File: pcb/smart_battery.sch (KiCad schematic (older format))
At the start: 37 parts, among them J11 Conn_01x05_RTC, J12 Conn_HtrTh, J13 Conn_BattTh, Q1 MMBT5551L, Q2 MMBT5551L, U1 SPX3819M5-L-3-3, U10 FEATHER_M0_ADALOGGER, U11 FEATHERWING_HEATER_RELAY, U12 FEATHERWING_ETHERNET, U13 FEATHERWING_MINI_RELAY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

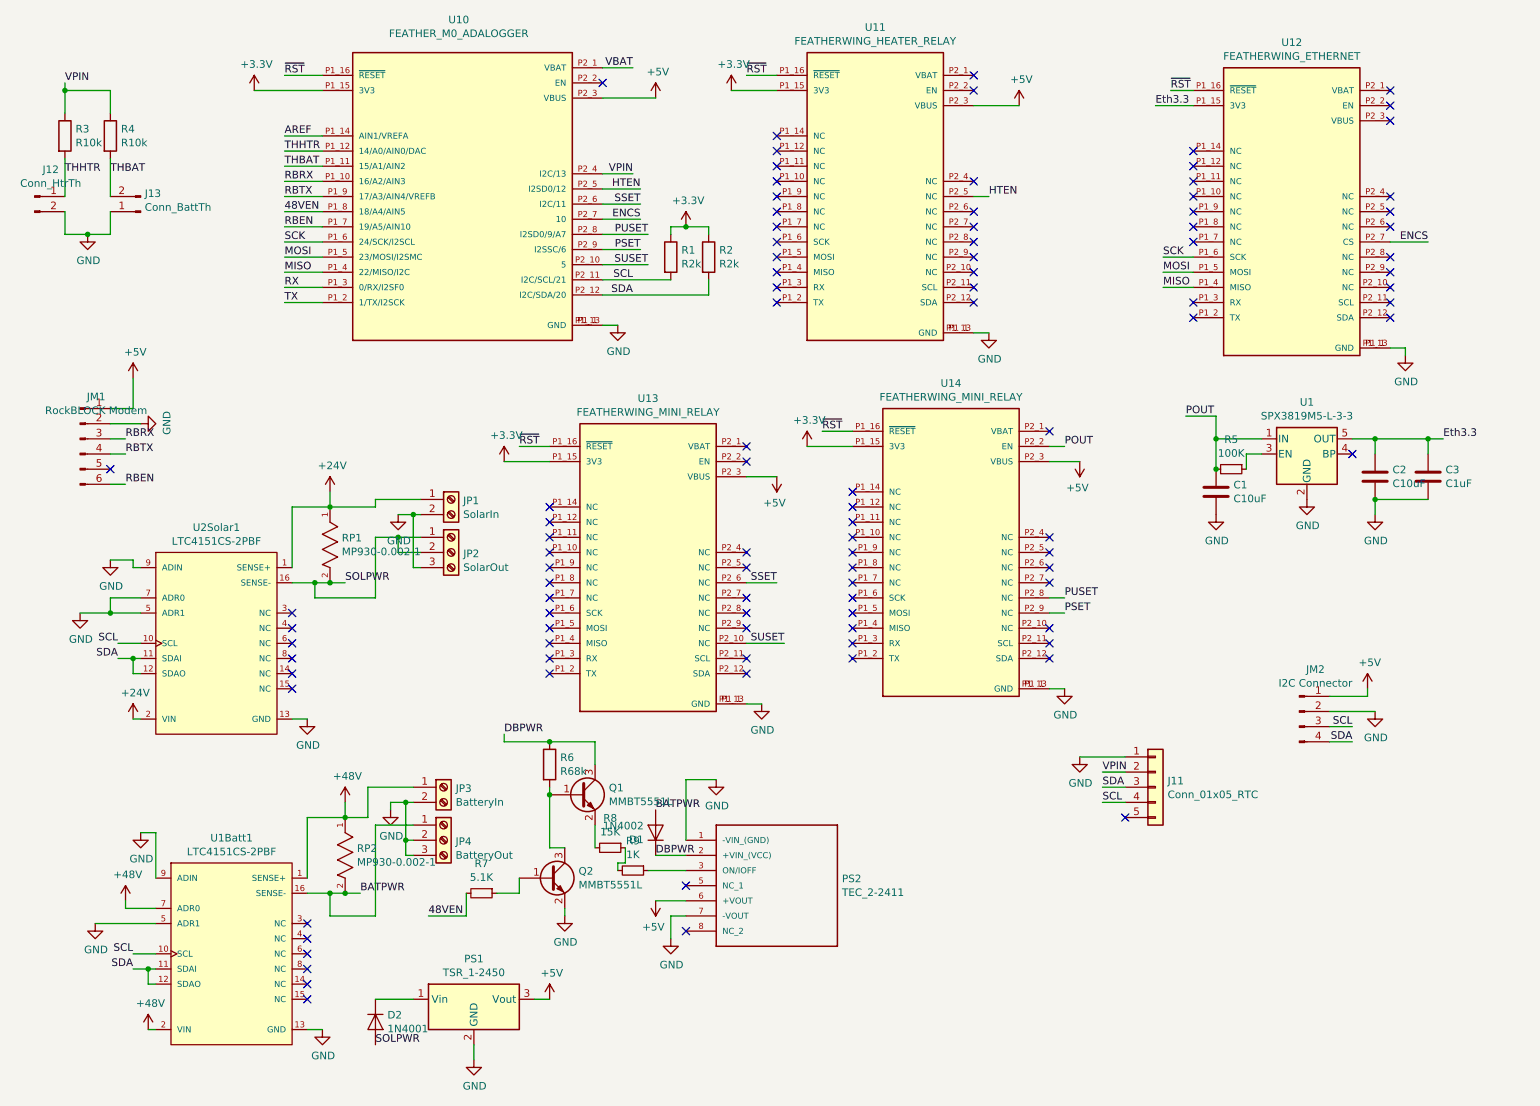
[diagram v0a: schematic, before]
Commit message: Fixed Sean comments, still need to redo the PCB
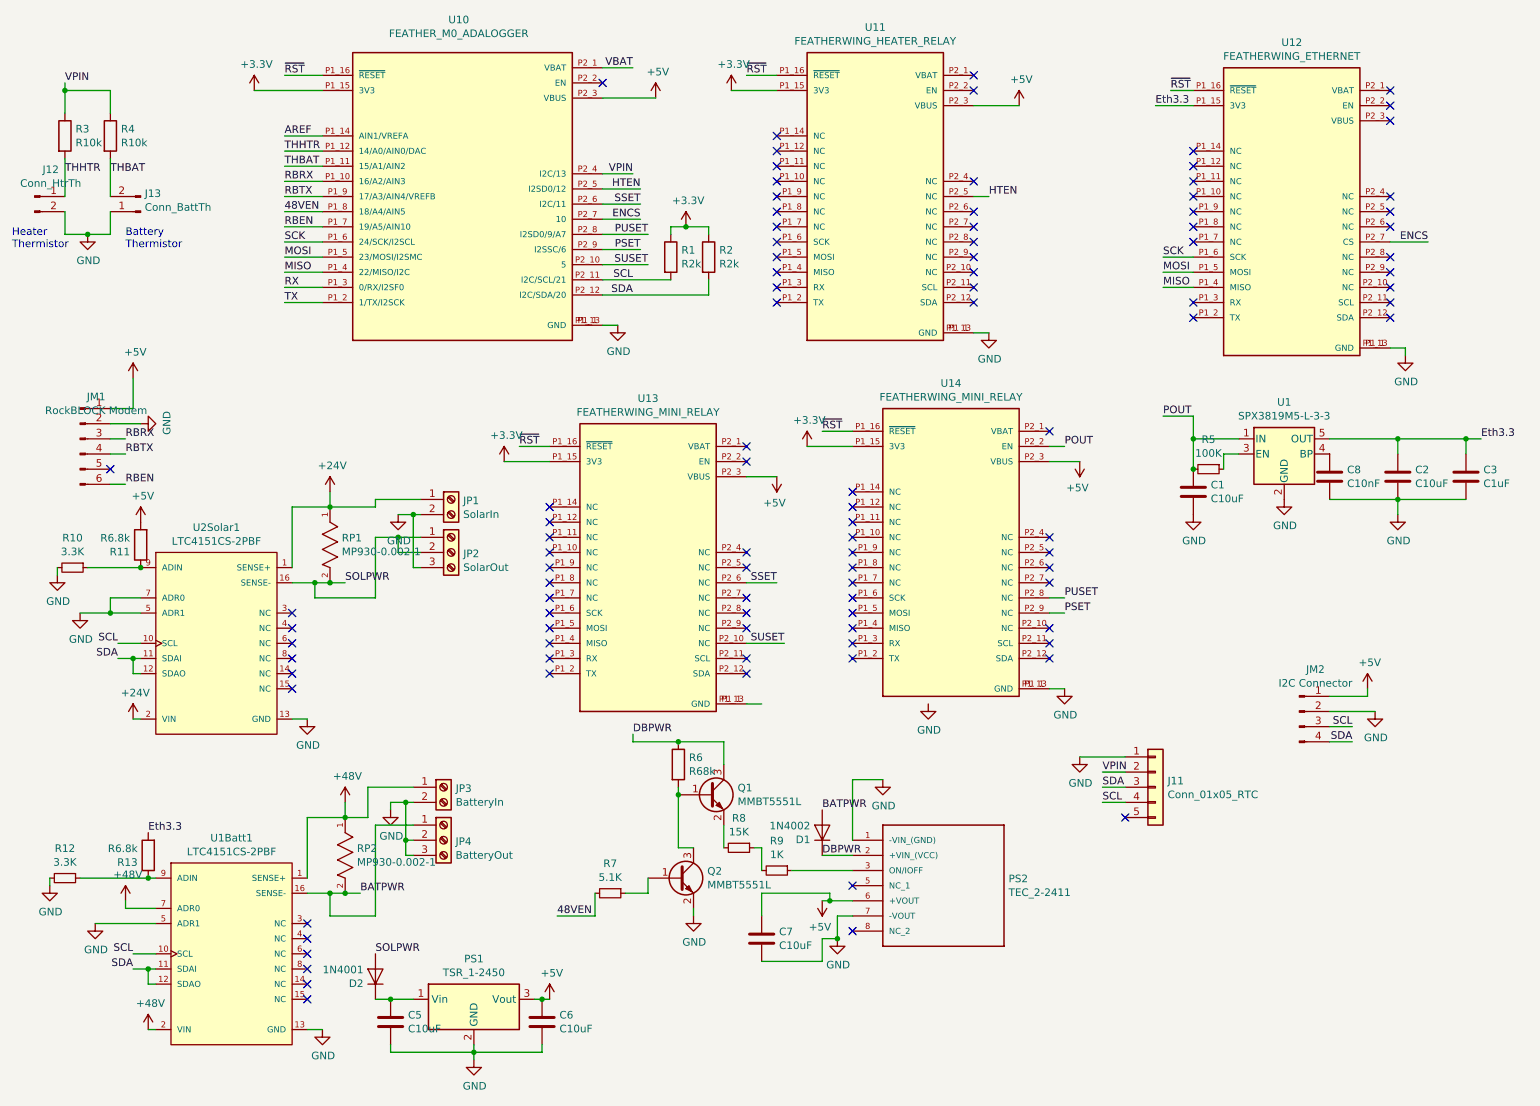
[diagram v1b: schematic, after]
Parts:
- added C5, C6, C7: C10uF, Capacitor_SMD:C_0805_2012Metric, symbol Device:C
- added C8: C10nF, Capacitor_SMD:C_0805_2012Metric, symbol Device:C
- added R10, R12: 3.3K, Resistor_SMD:R_0805_2012Metric, symbol Device:R_Small
- added R11, R13: R6.8k, Resistor_SMD:R_0805_2012Metric, symbol Device:R
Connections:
- net +5V: now also C6.1, C7.1, R11.2
- net Eth3.3: now also R13.2
- net GND: now also C5.2, C6.2, C7.2, C8.2, R10.2, R12.2; no longer U13.P1_1 (GND), U13.P1_13 (GND), U1Batt1.9 (ADIN), U2Solar1.9 (ADIN)
- net at U1.4 (BP): now also C8.1
- net at D2.1 (K), PS1.1 (Vin): now also C5.1
- new net: R12.1, R13.1, U1Batt1.9 (ADIN)
- new net: R10.1, R11.1, U2Solar1.9 (ADIN)
- new net: U13.P1_1 (GND), U13.P1_13 (GND)
- no-connect marks 101 -> 100
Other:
- note added: "Battery\nThermistor\n"
- note added: "Heater\nThermistor\n"
- moved on the sheet: C1, C2, C3, D1, D2, PS2, Q1, Q2, R5, R6, R7, R8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

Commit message: Added power symbols instead of labels for power buses
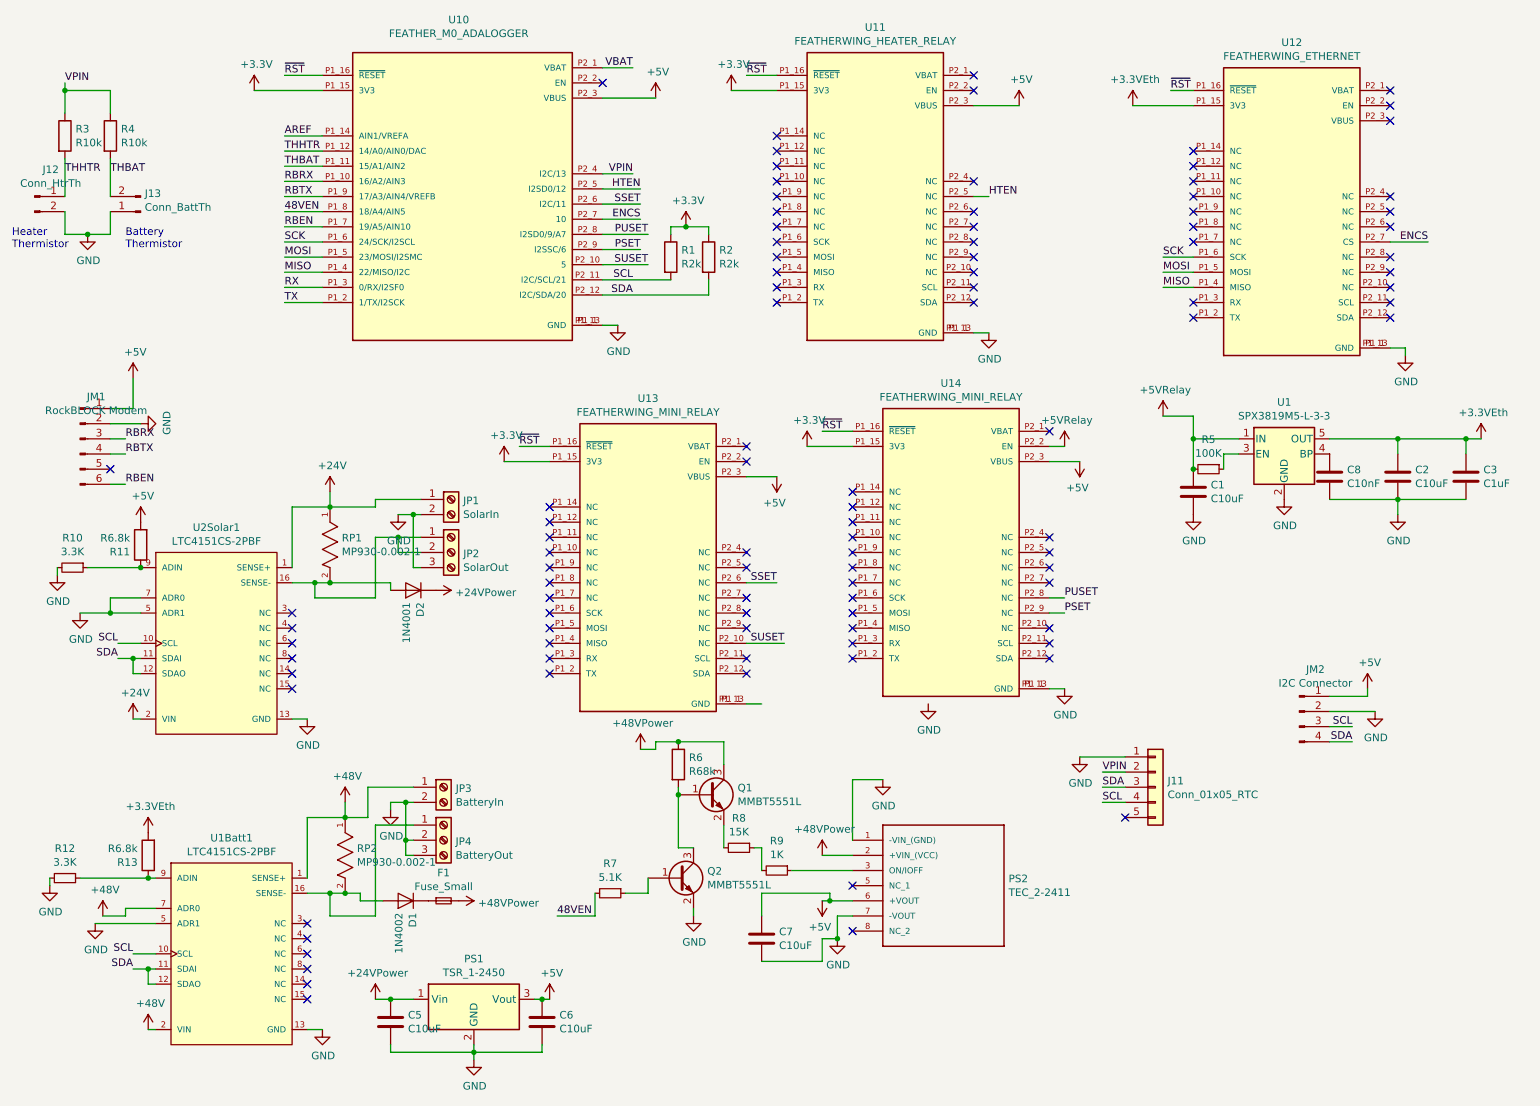
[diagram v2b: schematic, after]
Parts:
- added F1: Fuse_Small, symbol Device:Fuse_Small
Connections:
- net Eth3.3 is gone; now on net +48V: C2.1, C3.1, R13.2, U1.5 (OUT), U12.P1_15 (3V3)
- net POUT is gone; now on net +48V: C1.1, R5.2, U1.1 (IN), U14.P2_2 (EN)
- net +48V: now also C5.1, D2.1 (K), PS1.1 (Vin), PS2.2 (+VIN_(VCC)), Q1.3 (C), R6.1, F1.2
- net BATPWR: no longer names the net of D1.2 (A), JP4.1 (Pin_1), RP2.2, U1Batt1.16 (SENSE-)
- removed net DBPWR: D1.1 (K), PS2.2 (+VIN_(VCC)), Q1.3 (C), R6.1
- net SOLPWR: no longer names the net of D2.2 (A), JP2.1 (Pin_1), JP2.2 (Pin_2), RP1.2, U2Solar1.16 (SENSE-)
- new net: D1.1 (K), F1.1
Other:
- moved on the sheet: D1, D2
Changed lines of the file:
@@
 L power:+48V #PWR05
 U 1 1 6010A445
-P 1300 6400
-F 0 "#PWR05" H 1300 6250 50  0001 C CNN
-F 1 "+48V" H 1315 6573 50  0000 C CNN
-F 2 "" H 1300 6400 50  0001 C CNN
-F 3 "" H 1300 6400 50  0001 C CNN
-	1    1300 6400
-	1    0    0    -1
-$EndComp
-Wire Wire Line
-	1300 6400 1300 6450
+P 1150 6500
+F 0 "#PWR05" H 1150 6350 50  0001 C CNN
+F 1 "+48V" H 1165 6673 50  0000 C CNN
+F 2 "" H 1150 6500 50  0001 C CNN
+F 3 "" H 1150 6500 50  0001 C CNN
+	1    1150 6500
+	1    0    0    -1
+$EndComp
 Wire Wire Line
 	1300 6450 1500 6450
@@
 	-1   0    0    1
 $EndComp
-Text Label 7500 3400 0    50   ~ 0
-POUT
 $Comp
 L Connector_Generic:Conn_01x05 J11
@@
 Wire Wire Line
 	10250 3350 10150 3350
-Text Label 8100 1150 0    50   ~ 0
-Eth3.3
 $Comp
 L Device:R_Small R5
@@
 	1    0    0    -1
 $EndComp
-Text Label 8150 3200 0    50   ~ 0
-POUT
 Wire Wire Line
 	8150 3200 8350 3200
@@
 	2850 6350 2750 6350
 Connection ~ 2750 6350
-Text Label 5900 5800 0    50   ~ 0
-BATPWR
-Text Label 2850 6350 0    50   ~ 0
-BATPWR
-Text Label 2750 4300 0    50   ~ 0
-SOLPWR
-Wire Wire Line
-	2750 4300 2650 4300
 Connection ~ 2650 4300
-Text Label 2950 6750 0    50   ~ 0
-SOLPWR
 Wire Wire Line
 	2950 7050 3050 7050
@@
 	1    0    0    -1
 $EndComp
-Wire Wire Line
-	4650 5300 4650 5350
-Wire Wire Line
-	4650 5350 4950 5350
 $Comp
 L Device:R R6
@@
 Wire Wire Line
 	5250 5350 5250 5500
-Connection ~ 4950 5350
 $Comp
 L power:+5V #PWR0104
@@
 Wire Wire Line
 	8350 1050 8200 1050
-Wire Wire Line
-	8350 1150 8100 1150
 NoConn ~ 6900 950
 NoConn ~ 9650 1050
@@
 L Diode:1N4001 D2
 U 1 1 60267D7A
-P 2950 6900
-F 0 "D2" V 2904 6979 50  0000 L CNN
-F 1 "1N4001" V 2995 6979 50  0000 L CNN
-F 2 "Diode_THT:D_DO-41_SOD81_P10.16mm_Horizontal" H 2950 6725 50  0001 C CNN
-F 3 "http://www.vishay.com/docs/88503/1n4001.pdf" H 2950 6900 50  0001 C CNN
-	1    2950 6900
-	0    -1   -1   0
+P 3200 4350
+F 0 "D2" V 3154 4429 50  0000 L CNN
+F 1 "1N4001" V 3245 4429 50  0000 L CNN
+F 2 "Diode_THT:D_DO-41_SOD81_P10.16mm_Horizontal" H 3200 4175 50  0001 C CNN
+F 3 "http://www.vishay.com/docs/88503/1n4001.pdf" H 3200 4350 50  0001 C CNN
+	1    3200 4350
+	-1   0    0    1
 $EndComp
 $Comp
 L Diode:1N4002 D1
 U 1 1 602681D6
-P 5900 5950
-F 0 "D1" V 5854 6029 50  0000 L CNN
-F 1 "1N4002" V 5945 6029 50  0000 L CNN
-F 2 "Diode_THT:D_DO-41_SOD81_P10.16mm_Horizontal" H 5900 5775 50  0001 C CNN
-F 3 "http://www.vishay.com/docs/88503/1n4001.pdf" H 5900 5950 50  0001 C CNN
-	1    5900 5950
-	0    -1   -1   0
-$EndComp
-Text Label 4650 5300 0    50   ~ 0
-DBPWR
-Text Label 5900 6100 0    50   ~ 0
-DBPWR
+P 3150 6400
+F 0 "D1" V 3104 6479 50  0000 L CNN
+F 1 "1N4002" V 3195 6479 50  0000 L CNN
+F 2 "Diode_THT:D_DO-41_SOD81_P10.16mm_Horizontal" H 3150 6225 50  0001 C CNN
+F 3 "http://www.vishay.com/docs/88503/1n4001.pdf" H 3150 6400 50  0001 C CNN
+	1    3150 6400
+	-1   0    0    1
+$EndComp
 Wire Wire Line
 	4950 5700 4950 6050
@@
 	1450 6250 1500 6250
 Connection ~ 1450 6250
-Text Label 10250 3350 0    50   ~ 0
-Eth3.3
-Text Label 1450 5950 0    50   ~ 0
-Eth3.3
+Wire Wire Line
+	2850 6350 2850 6400
+$Comp
+L eec:+48VPower #PWR?
+U 1 1 603099AD
+P 5900 6100
+F 0 "#PWR?" H 5900 5950 50  0001 C CNN
+F 1 "+48VPower" H 5915 6273 50  0000 C CNN
+F 2 "" H 5900 6100 50  0001 C CNN
+F 3 "" H 5900 6100 50  0001 C CNN
+	1    5900 6100
+	1    0    0    -1
+$EndComp
+Wire Wire Line
+	2850 6400 3000 6400
+$Comp
+L Device:Fuse_Small F1
+U 1 1 60316340
+P 3400 6400
+F 0 "F1" H 3400 6585 50  0000 C CNN
+F 1 "Fuse_Small" H 3400 6494 50  0000 C CNN
+F 2 "" H 3400 6400 50  0001 C CNN
+F 3 "~" H 3400 6400 50  0001 C CNN
+	1    3400 6400
+	1    0    0    -1
+$EndComp
+$Comp
+L eec:+48VPower #PWR?
+U 1 1 60316928
+P 3500 6400
+F 0 "#PWR?" H 3500 6250 50  0001 C CNN
+F 1 "+48VPower" V 3515 6528 50  0000 L CNN
+F 2 "" H 3500 6400 50  0001 C CNN
+F 3 "" H 3500 6400 50  0001 C CNN
+	1    3500 6400
+	0    1    1    0
+$EndComp
+$Comp
+L eec:+48VPower #PWR?
+U 1 1 60316F04
+P 4700 5400
+F 0 "#PWR?" H 4700 5250 50  0001 C CNN
+F 1 "+48VPower" H 4715 5573 50  0000 C CNN
+F 2 "" H 4700 5400 50  0001 C CNN
+F 3 "" H 4700 5400 50  0001 C CNN
+	1    4700 5400
+	1    0    0    -1
+$EndComp
+Wire Wire Line
+	4700 5400 4800 5400
+Wire Wire Line
+	4800 5400 4800 5350
+Wire Wire Line
+	4800 5350 4950 5350
+Connection ~ 4950 5350
+Wire Wire Line
+	3050 4300 3050 4350
+Wire Wire Line
+	2650 4300 3050 4300
+$Comp
+L eec:+24VPower #PWR?
+U 1 1 6033DA59
+P 3350 4350
+F 0 "#PWR?" H 3350 4200 50  0001 C CNN
+F 1 "+24VPower" V 3365 4478 50  0000 L CNN
+F 2 "" H 3350 4350 50  0001 C CNN
+F 3 "" H 3350 4350 50  0001 C CNN
+	1    3350 4350
+	0    1    1    0
+$EndComp
+$Comp
+L eec:+24VPower #PWR?
+U 1 1 6033E548
+P 2950 7050
+F 0 "#PWR?" H 2950 6900 50  0001 C CNN
+F 1 "+24VPower" H 2965 7223 50  0000 C CNN
+F 2 "" H 2950 7050 50  0001 C CNN
+F 3 "" H 2950 7050 50  0001 C CNN
+	1    2950 7050
+	1    0    0    -1
+$EndComp
+Wire Wire Line
+	1300 6450 1300 6500
+Wire Wire Line
+	1300 6500 1150 6500
+$Comp
+L eec:+5VRelay #PWR?
+U 1 1 6038C736
+P 7500 3400
+F 0 "#PWR?" H 7500 3250 50  0001 C CNN
+F 1 "+5VRelay" H 7515 3573 50  0000 C CNN
+F 2 "" H 7500 3400 50  0001 C CNN
+F 3 "" H 7500 3400 50  0001 C CNN
+	1    7500 3400
+	1    0    0    -1
+$EndComp
+$Comp
+L eec:+5VRelay #PWR?
+U 1 1 6038C83C
+P 8150 3200
+F 0 "#PWR?" H 8150 3050 50  0001 C CNN
+F 1 "+5VRelay" H 8165 3373 50  0000 C CNN
+F 2 "" H 8150 3200 50  0001 C CNN
+F 3 "" H 8150 3200 50  0001 C CNN
+	1    8150 3200
+	1    0    0    -1
+$EndComp
+$Comp
+L eec:+3.3VEth #PWR?
+U 1 1 6039A381
+P 10250 3350
+F 0 "#PWR?" H 10250 3200 50  0001 C CNN
+F 1 "+3.3VEth" H 10265 3523 50  0000 C CNN
+F 2 "" H 10250 3350 50  0001 C CNN
+F 3 "" H 10250 3350 50  0001 C CNN
+	1    10250 3350
+	1    0    0    -1
+$EndComp
+$Comp
+L eec:+3.3VEth #PWR?
+U 1 1 6039A683
+P 1450 5950
+F 0 "#PWR?" H 1450 5800 50  0001 C CNN
+F 1 "+3.3VEth" H 1465 6123 50  0000 C CNN
+F 2 "" H 1450 5950 50  0001 C CNN
+F 3 "" H 1450 5950 50  0001 C CNN
+	1    1450 5950
+	1    0    0    -1
+$EndComp
+$Comp
+L eec:+3.3VEth #PWR?
+U 1 1 6039AA3D
+P 7950 1150
+F 0 "#PWR?" H 7950 1000 50  0001 C CNN
+F 1 "+3.3VEth" H 7965 1323 50  0000 C CNN
+F 2 "" H 7950 1150 50  0001 C CNN
+F 3 "" H 7950 1150 50  0001 C CNN
+	1    7950 1150
+	1    0    0    -1
+$EndComp
+Wire Wire Line
+	7950 1150 8350 1150
 $EndSCHEMATC

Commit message: Routed the new layout just need ground plane
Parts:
- added F2: Fuse_Small, Fuse:Fuseholder_Cylinder-5x20mm_Schurter_0031_8201_Horizontal_Open, symbol Device:Fuse_Small
- F1: footprint (none) -> Fuse:Fuseholder_Cylinder-5x20mm_Schurter_0031_8201_Horizontal_Open
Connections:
- net +48V: now also F2.1; no longer D2.1 (K)
- new net: D2.1 (K), F2.2
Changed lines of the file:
@@
 $EndComp
 $Comp
-L power:GND #PWR?
+L power:GND #PWR0117
 U 1 1 60405690
 P 800 6300
-F 0 "#PWR?" H 800 6050 50  0001 C CNN
+F 0 "#PWR0117" H 800 6050 50  0001 C CNN
 F 1 "GND" H 805 6127 50  0000 C CNN
 F 2 "" H 800 6300 50  0001 C CNN
@@
 	2850 6350 2850 6400
 $Comp
-L eec:+48VPower #PWR?
+L eec:+48VPower #PWR0118
 U 1 1 603099AD
 P 5900 6100
-F 0 "#PWR?" H 5900 5950 50  0001 C CNN
+F 0 "#PWR0118" H 5900 5950 50  0001 C CNN
 F 1 "+48VPower" H 5915 6273 50  0000 C CNN
 F 2 "" H 5900 6100 50  0001 C CNN
@@
 F 0 "F1" H 3400 6585 50  0000 C CNN
 F 1 "Fuse_Small" H 3400 6494 50  0000 C CNN
-F 2 "" H 3400 6400 50  0001 C CNN
+F 2 "Fuse:Fuseholder_Cylinder-5x20mm_Schurter_0031_8201_Horizontal_Open" H 3400 6400 50  0001 C CNN
 F 3 "~" H 3400 6400 50  0001 C CNN
 	1    3400 6400
@@
 $EndComp
 $Comp
-L eec:+48VPower #PWR?
+L eec:+48VPower #PWR0119
 U 1 1 60316928
 P 3500 6400
-F 0 "#PWR?" H 3500 6250 50  0001 C CNN
+F 0 "#PWR0119" H 3500 6250 50  0001 C CNN
 F 1 "+48VPower" V 3515 6528 50  0000 L CNN
 F 2 "" H 3500 6400 50  0001 C CNN
@@
 $EndComp
 $Comp
-L eec:+48VPower #PWR?
+L eec:+48VPower #PWR0120
 U 1 1 60316F04
 P 4700 5400
-F 0 "#PWR?" H 4700 5250 50  0001 C CNN
+F 0 "#PWR0120" H 4700 5250 50  0001 C CNN
 F 1 "+48VPower" H 4715 5573 50  0000 C CNN
 F 2 "" H 4700 5400 50  0001 C CNN
@@
 	2650 4300 3050 4300
 $Comp
-L eec:+24VPower #PWR?
+L eec:+24VPower #PWR0121
 U 1 1 6033DA59
-P 3350 4350
-F 0 "#PWR?" H 3350 4200 50  0001 C CNN
-F 1 "+24VPower" V 3365 4478 50  0000 L CNN
-F 2 "" H 3350 4350 50  0001 C CNN
-F 3 "" H 3350 4350 50  0001 C CNN
-	1    3350 4350
+P 3400 4750
+F 0 "#PWR0121" H 3400 4600 50  0001 C CNN
+F 1 "+24VPower" V 3415 4878 50  0000 L CNN
+F 2 "" H 3400 4750 50  0001 C CNN
+F 3 "" H 3400 4750 50  0001 C CNN
+	1    3400 4750
 	0    1    1    0
 $EndComp
 $Comp
-L eec:+24VPower #PWR?
+L eec:+24VPower #PWR0122
 U 1 1 6033E548
 P 2950 7050
-F 0 "#PWR?" H 2950 6900 50  0001 C CNN
+F 0 "#PWR0122" H 2950 6900 50  0001 C CNN
 F 1 "+24VPower" H 2965 7223 50  0000 C CNN
 F 2 "" H 2950 7050 50  0001 C CNN
@@
 	1300 6500 1150 6500
 $Comp
-L eec:+5VRelay #PWR?
+L eec:+5VRelay #PWR0123
 U 1 1 6038C736
 P 7500 3400
-F 0 "#PWR?" H 7500 3250 50  0001 C CNN
+F 0 "#PWR0123" H 7500 3250 50  0001 C CNN
 F 1 "+5VRelay" H 7515 3573 50  0000 C CNN
 F 2 "" H 7500 3400 50  0001 C CNN
@@
 $EndComp
 $Comp
-L eec:+5VRelay #PWR?
+L eec:+5VRelay #PWR0124
 U 1 1 6038C83C
 P 8150 3200
-F 0 "#PWR?" H 8150 3050 50  0001 C CNN
+F 0 "#PWR0124" H 8150 3050 50  0001 C CNN
 F 1 "+5VRelay" H 8165 3373 50  0000 C CNN
 F 2 "" H 8150 3200 50  0001 C CNN
@@
 $EndComp
 $Comp
-L eec:+3.3VEth #PWR?
+L eec:+3.3VEth #PWR0125
 U 1 1 6039A381
 P 10250 3350
-F 0 "#PWR?" H 10250 3200 50  0001 C CNN
+F 0 "#PWR0125" H 10250 3200 50  0001 C CNN
 F 1 "+3.3VEth" H 10265 3523 50  0000 C CNN
 F 2 "" H 10250 3350 50  0001 C CNN
@@
 $EndComp
 $Comp
-L eec:+3.3VEth #PWR?
+L eec:+3.3VEth #PWR0126
 U 1 1 6039A683
 P 1450 5950
-F 0 "#PWR?" H 1450 5800 50  0001 C CNN
+F 0 "#PWR0126" H 1450 5800 50  0001 C CNN
 F 1 "+3.3VEth" H 1465 6123 50  0000 C CNN
 F 2 "" H 1450 5950 50  0001 C CNN
@@
 $EndComp
 $Comp
-L eec:+3.3VEth #PWR?
+L eec:+3.3VEth #PWR0127
 U 1 1 6039AA3D
 P 7950 1150
-F 0 "#PWR?" H 7950 1000 50  0001 C CNN
+F 0 "#PWR0127" H 7950 1000 50  0001 C CNN
 F 1 "+3.3VEth" H 7965 1323 50  0000 C CNN
 F 2 "" H 7950 1150 50  0001 C CNN
@@
 Wire Wire Line
 	7950 1150 8350 1150
+$Comp
+L Device:Fuse_Small F2
+U 1 1 6031234C
+P 3550 4400
+F 0 "F2" H 3550 4585 50  0000 C CNN
+F 1 "Fuse_Small" H 3550 4494 50  0000 C CNN
+F 2 "Fuse:Fuseholder_Cylinder-5x20mm_Schurter_0031_8201_Horizontal_Open" H 3550 4400 50  0001 C CNN
+F 3 "~" H 3550 4400 50  0001 C CNN
+	1    3550 4400
+	-1   0    0    1
+$EndComp
+Wire Wire Line
+	3350 4350 3450 4350
+Wire Wire Line
+	3450 4350 3450 4400
+Wire Wire Line
+	3650 4400 3800 4400
+Wire Wire Line
+	3800 4400 3800 4650
+Wire Wire Line
+	3800 4650 3400 4650
+Wire Wire Line
+	3400 4650 3400 4750
 $EndSCHEMATC
